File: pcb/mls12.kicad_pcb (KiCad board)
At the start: 4 copper layers, 130 x 40 mm, 137 parts, among them J1 MTJ-88ARX1-FSM-LG, J2 TC2070-FP, J3 SM04B-SRSS-TB, J4 JST B3B-ZR, J5 DC barrel plug, J6 JST B3B-ZR, J7 DC barrel plug, Q1 DMG3406L, Q2 DMG3406L, Q3 DMG3406L, Q4 DMG3406L, U1 DPC817S-C-TR, U2 KSZ8081RNA, U3 LMR51606XDBVR, U4 STM32H563RIT6, U5 W25Q16JVSS, Y1 25MHz, Y2 25MHz

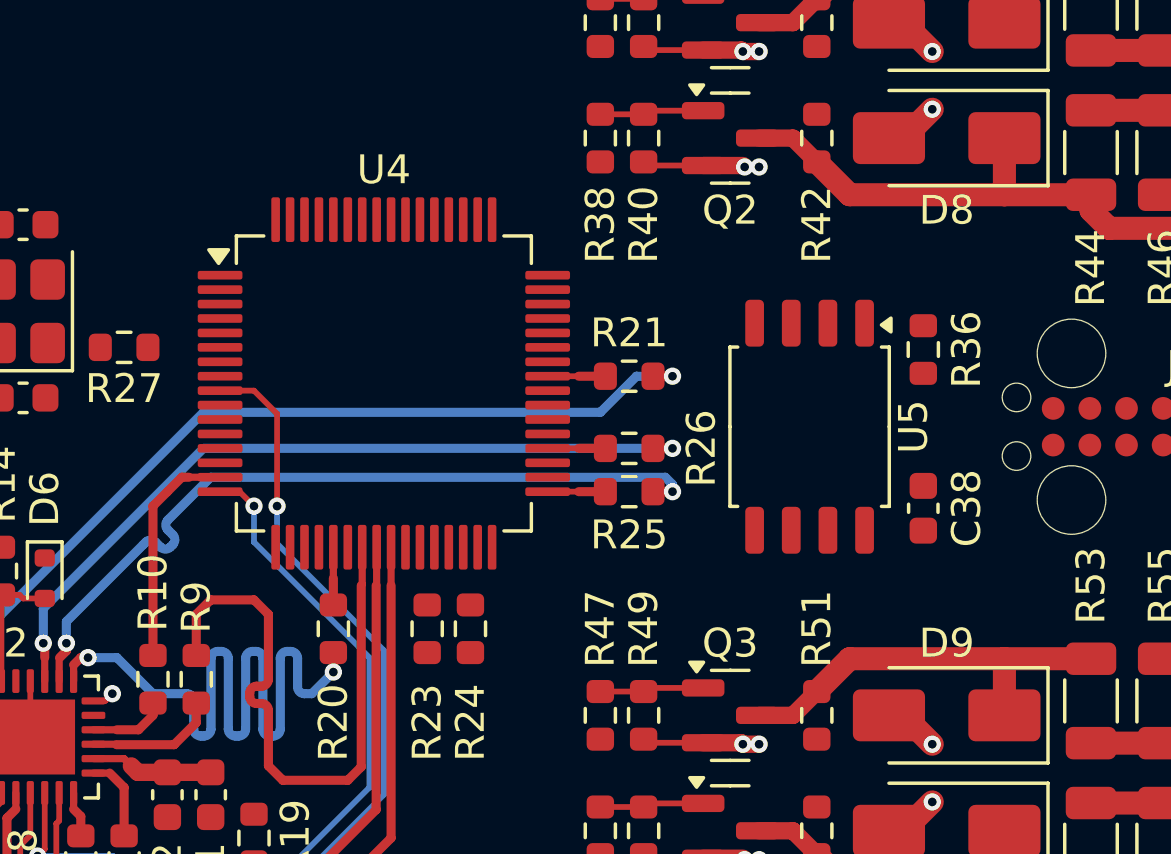
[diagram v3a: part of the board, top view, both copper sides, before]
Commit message: Route NOR flash QSPI traces
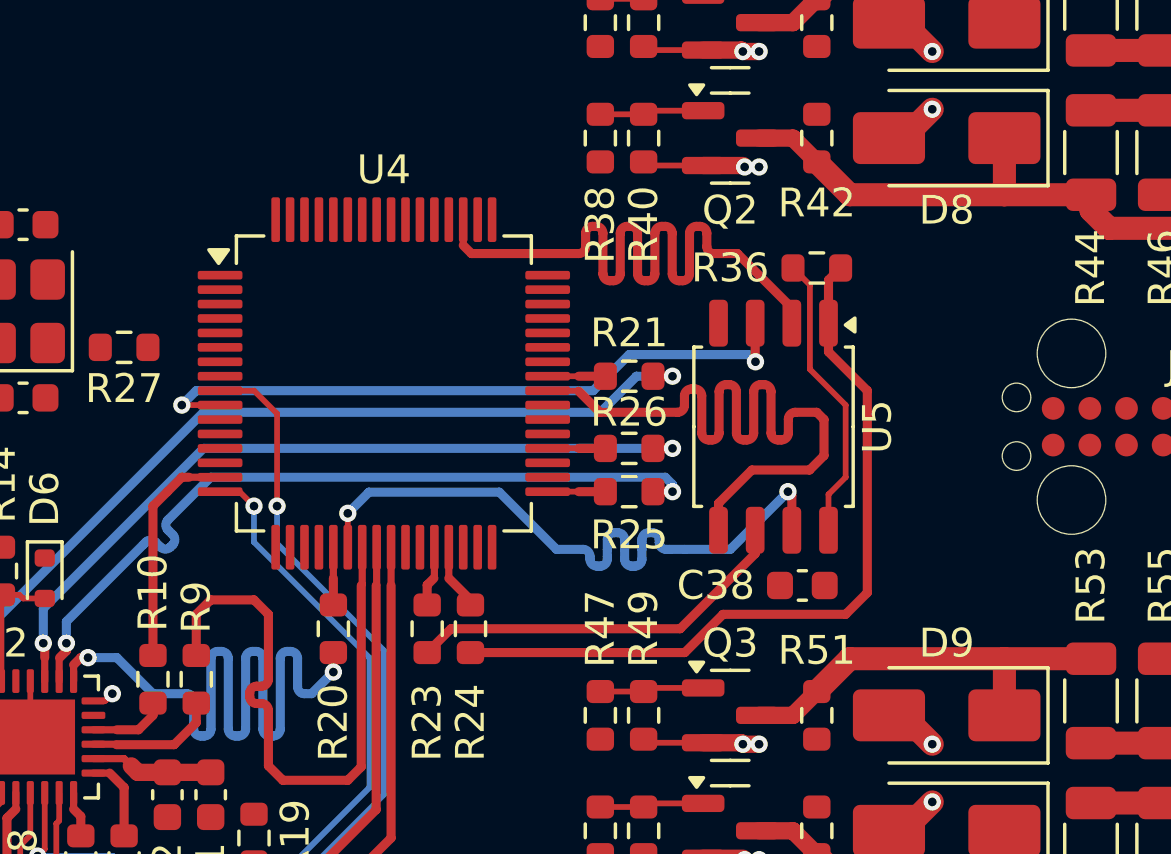
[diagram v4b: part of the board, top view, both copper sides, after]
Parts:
- moved C38 4.97 mm to (207.0, 105.5), turned to 180 degrees
- moved R36 4.65 mm to (207.5, 94.5), turned to 0 degrees
- moved U5 1.25 mm to (206.0, 100.0)
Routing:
- net /MCU/FLASH.~{CS}: track 0.00 -> 26.6 mm
- net /MCU/FLASH.IO_{0}: track 0.00 -> 26.1 mm
- net /MCU/FLASH.IO_{1}: track 0.00 -> 25.1 mm
- net /MCU/FLASH.IO_{2}: track 0.00 -> 23.4 mm, vias 0 -> 2
- net /MCU/FLASH.IO_{3}: track 0.00 -> 23.3 mm, vias 0 -> 2
- net /MCU/FLASH.CLK: track 0.00 -> 13.6 mm
- net +3.3V: track 9.83 -> 19.9 mm
- net Net-(U4B-PB10): track 0.00 -> 2.31 mm
- net Net-(U4B-PB2): track 0.00 -> 2.10 mm

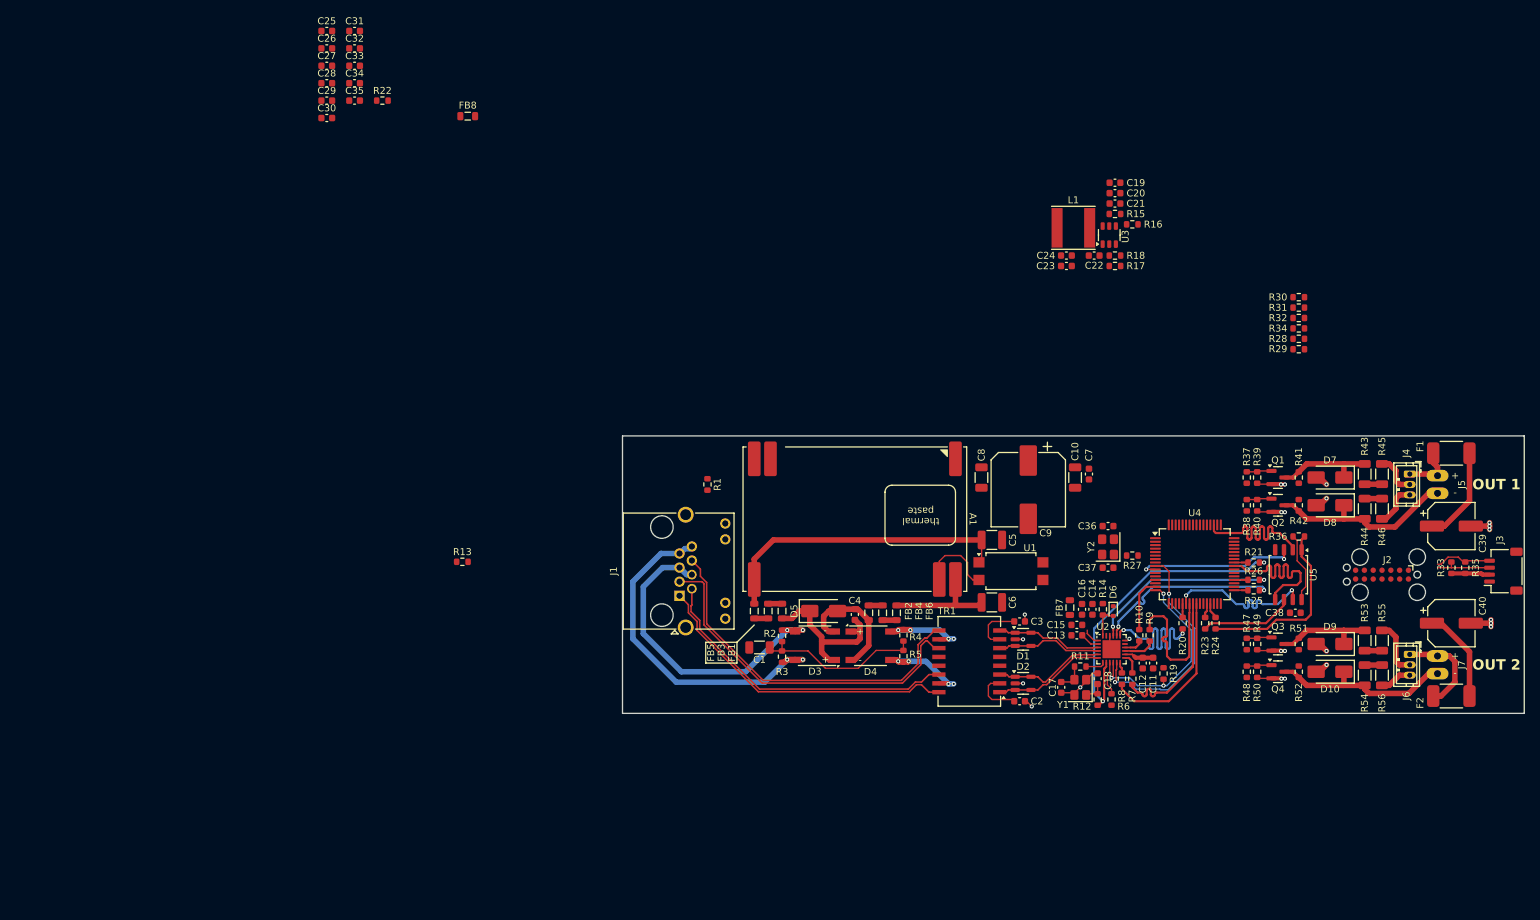
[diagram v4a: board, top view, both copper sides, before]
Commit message: Route MCU decoupling caps
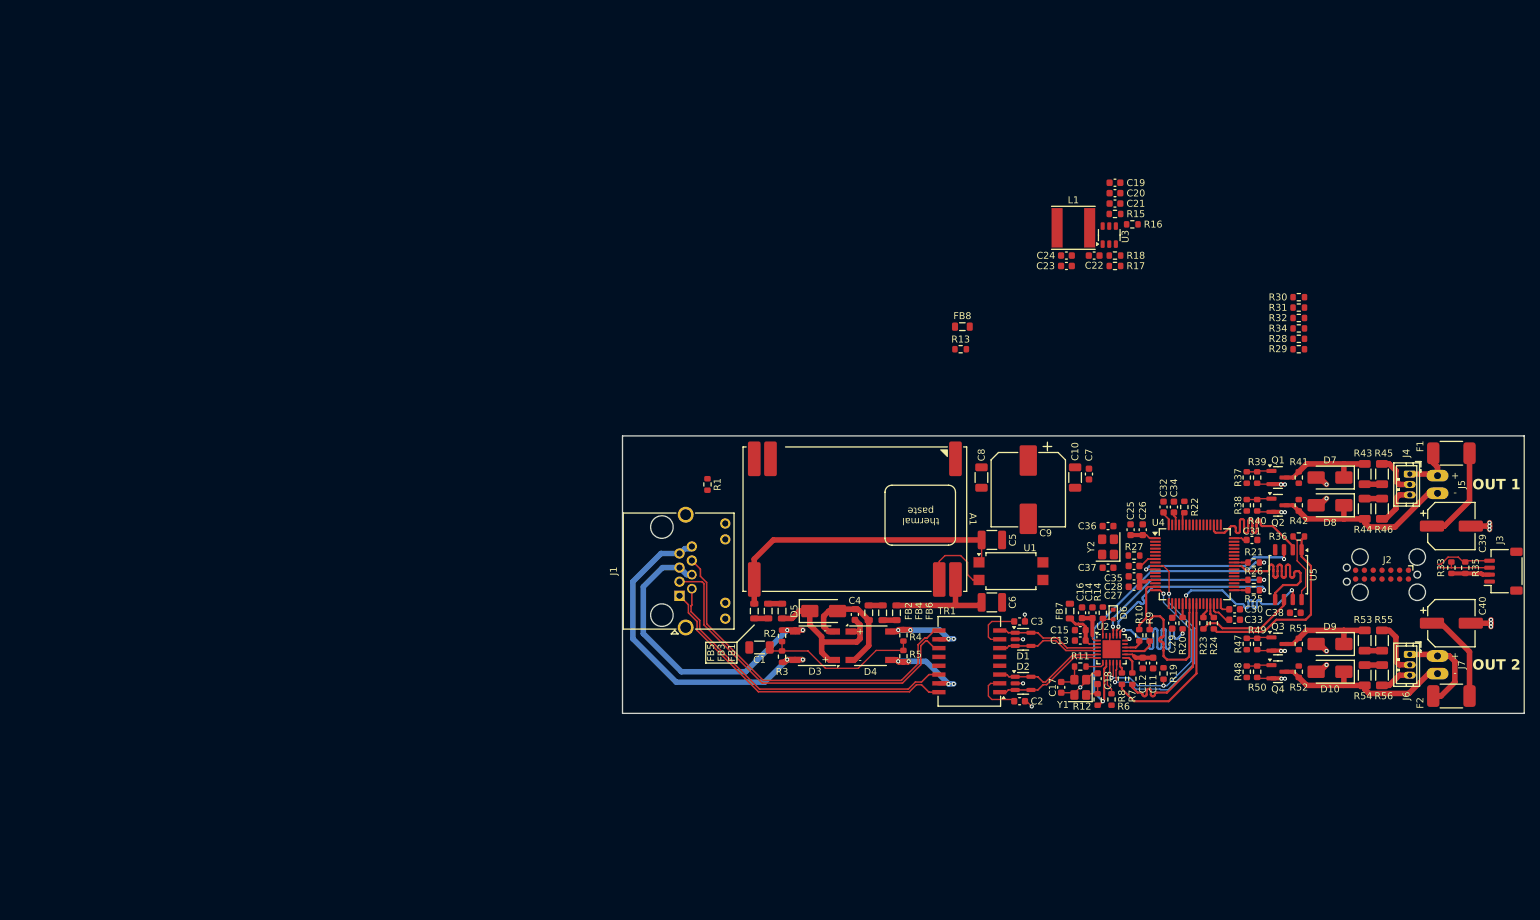
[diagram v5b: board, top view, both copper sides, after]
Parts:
- moved C33 149.9 mm to (198.2, 106.5)
- moved C30 148.8 mm to (198.2, 105.0)
- moved C31 148.7 mm to (200.8, 95.0)
- moved C29 143.3 mm to (189.2, 107.0), turned to -90 degrees
- moved C27 138.5 mm to (183.8, 101.8), turned to 180 degrees
- moved C26 136.6 mm to (185.0, 93.5), turned to 90 degrees
- moved C28 136.4 mm to (183.8, 100.2), turned to 180 degrees
- moved C25 136.4 mm to (183.2, 93.5), turned to 90 degrees
- moved C32 134.1 mm to (188.0, 90.2), turned to 90 degrees
- moved C34 133.0 mm to (189.5, 90.2), turned to 90 degrees
- moved C35 130.9 mm to (183.8, 98.8), turned to 180 degrees
- moved R22 129.6 mm to (191.0, 90.2), turned to 90 degrees
- moved R13 78.1 mm to (158.8, 67.5)
- moved FB8 77.5 mm to (159.0, 64.2)
- moved C13 0.90 mm to (176.0, 109.5)
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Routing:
- net /MCU/V_{t,ref}: track 0.00 -> 15.8 mm
- net Net-(U2-VDDA_3.3): track 2.81 -> 6.75 mm
- net Net-(C33-Pad1): track 0.00 -> 3.79 mm
- net Net-(U2-VDD_1.2): track 2.48 -> 5.39 mm
- net /MCU/~{RESET}: track 0.00 -> 2.71 mm
- net Net-(C34-Pad1): track 0.00 -> 1.90 mm
- net Net-(U4F-BOOT0): track 0.00 -> 1.85 mm
- net /MCU/FLASH.CLK: track 13.6 -> 14.5 mm
- net /MCU/FLASH.~{CS}: track 26.6 -> 27.2 mm
- net /ETH-PHY/~{RST}: track 4.54 -> 4.04 mm

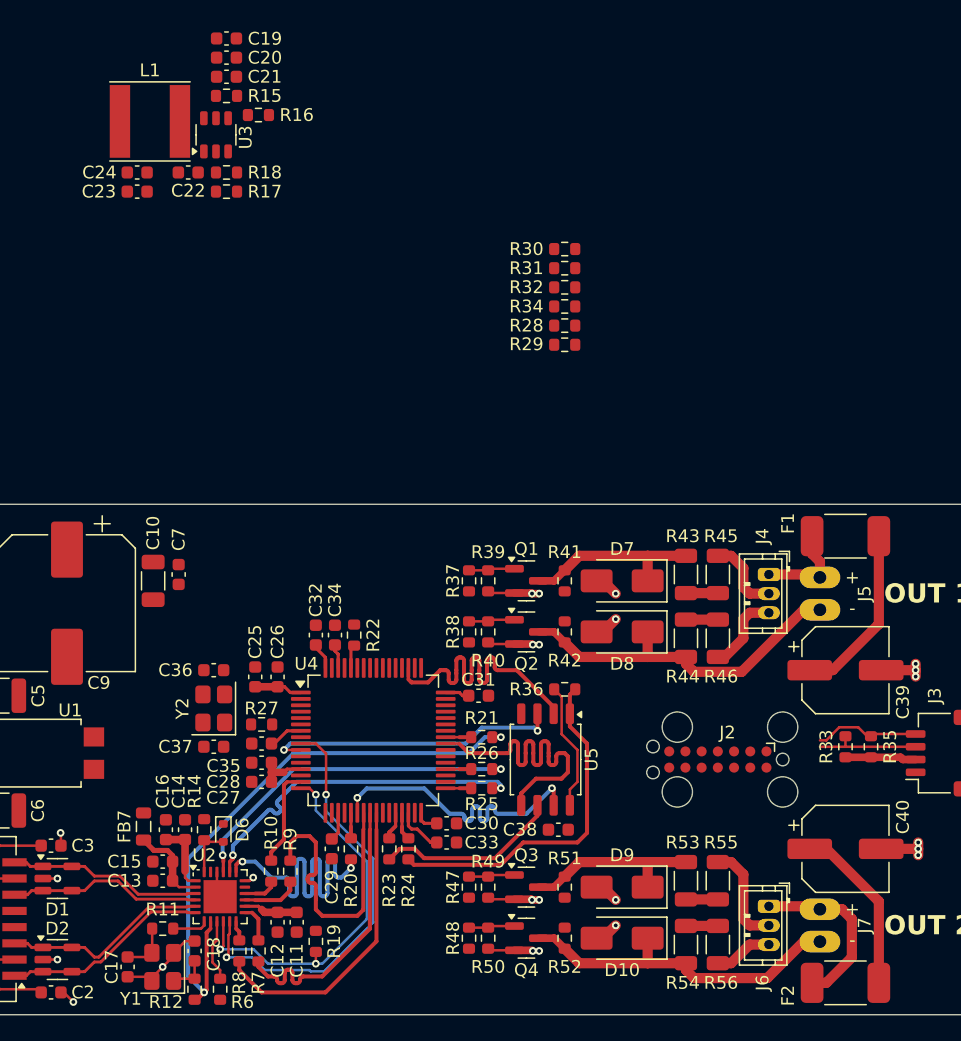
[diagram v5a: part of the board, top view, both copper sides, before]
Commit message: Layout buck converter, position TagConnect
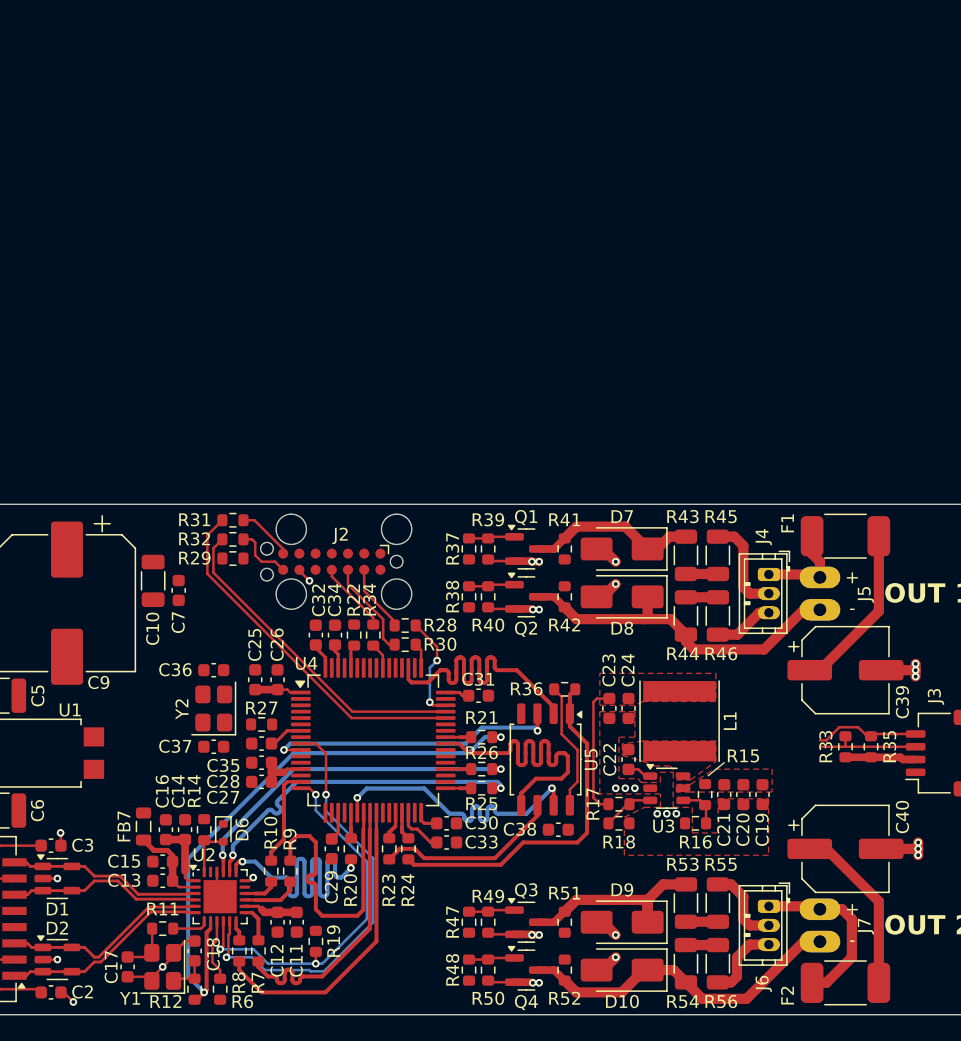
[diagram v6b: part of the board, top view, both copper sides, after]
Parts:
- moved C19 72.6 mm to (223.0, 102.8), turned to -90 degrees
- moved C20 70.5 mm to (221.5, 102.8), turned to -90 degrees
- moved C21 68.4 mm to (220.0, 102.8), turned to -90 degrees
- moved R15 66.4 mm to (218.5, 102.8), turned to -90 degrees
- moved R16 65.2 mm to (217.8, 105.0), turned to 180 degrees
- moved L1 62.7 mm to (216.5, 97.0), turned to 90 degrees
- moved U3 62.2 mm to (215.5, 102.2), turned to 0 degrees
- moved R18 59.6 mm to (211.8, 105.0), turned to 0 degrees
- moved C22 57.5 mm to (212.5, 100.0), turned to 90 degrees
- moved R17 57.0 mm to (211.8, 103.5)
- moved C24 57.0 mm to (212.5, 96.0), turned to -90 degrees
- moved C23 54.9 mm to (211.0, 96.0), turned to -90 degrees
- moved J2 34.0 mm to (189.2, 84.5)
- moved R30 33.4 mm to (195.0, 91.0), turned to 180 degrees
- moved R31 32.7 mm to (181.5, 81.2)
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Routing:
- net /MCU/DBG_UART_RX: track 0.00 -> 28.0 mm
- net /MCU/DBG_UART_TX: track 0.00 -> 25.6 mm
- net +3.3V: track 19.9 -> 30.2 mm
- net /MCU/SWDIO: track 0.00 -> 8.29 mm, vias 0 -> 2
- net Net-(J2-SWCLK): track 0.00 -> 7.64 mm
- net Net-(J2-SWO): track 0.00 -> 5.64 mm
- net Net-(J2-SWDIO): track 0.00 -> 5.35 mm
- net Net-(J2-RX): track 0.00 -> 4.69 mm
- net Net-(J2-TX): track 0.00 -> 4.41 mm
- net Net-(U3-FB): track 0.00 -> 4.02 mm
- net Net-(U3-EN): track 0.00 -> 3.31 mm
- net /MCU/SWO: track 0.00 -> 2.06 mm
- net /MCU/SWCLK: track 0.00 -> 2.00 mm
- net Net-(U3-CB): track 0.00 -> 1.92 mm
- net /LED output 2/LED_WW-: track 14.3 -> 16.1 mm
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- added copper zone on F.Cu, net +24V
- added copper zone on F.Cu, net +3.3V
- added copper zone on F.Cu, net GND
- added copper zone on F.Cu, net Net-(U3-SW)
